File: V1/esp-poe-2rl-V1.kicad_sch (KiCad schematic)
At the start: 68 parts, among them J1 USB_C_Receptacle_USB2.0, J2 1x2P 5,08mm, J3 1x2P 5,08mm, J4 RJ45 JACK, K1 G5NB-1A-E-DC5, K2 G5NB-1A-E-DC5, Q1 WPM2015-3/TR, Q2 LMUN2211LT1G, Q3 UMH3N, Q4 MMBT2222A, Q5 MMBT2222A, SW1 RESET, U1 CH340K, U2 ESP32-WROOM-32UE-N16, U3 LAN8710A

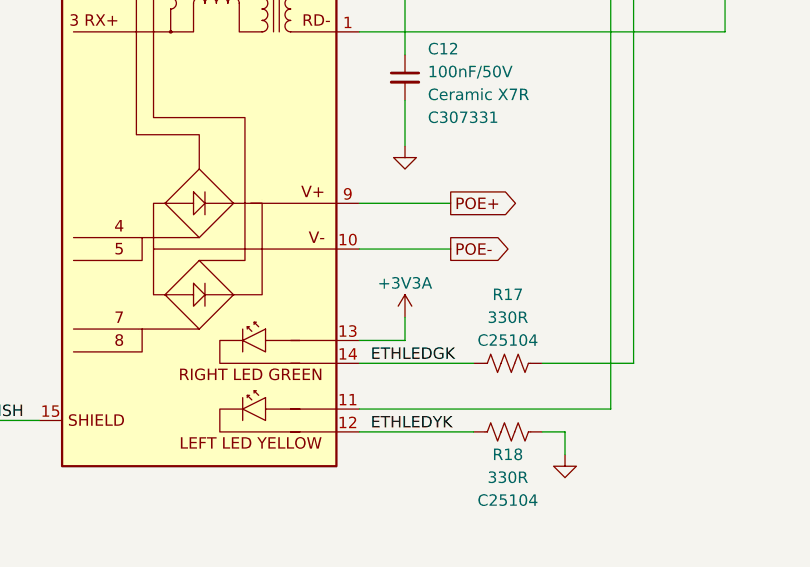
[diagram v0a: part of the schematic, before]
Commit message: Update power rail names
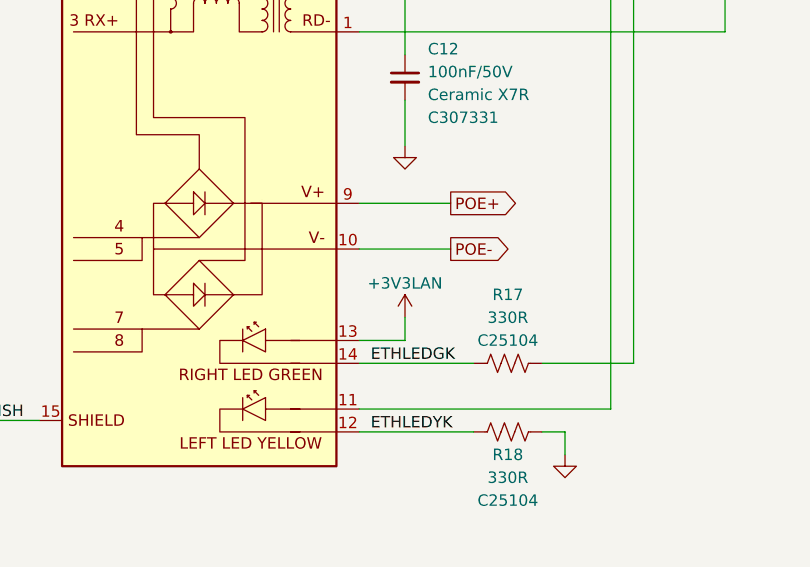
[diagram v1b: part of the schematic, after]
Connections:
- net +3V3A: no longer J4.13 (RLED+)
- net +3V3LAN: now also J4.13 (RLED+)
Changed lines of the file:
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@@
 	)
 	(symbol
+		(lib_id "Tales:+3V3LAN")
+		(at 336.55 219.71 0)
+		(unit 1)
+		(exclude_from_sim no)
+		(in_bom yes)
+		(on_board yes)
+		(dnp no)
+		(property "Reference" "#PWR042"
+			(at 336.55 223.52 0)
+			(effects
+				(font
+					(size 1.27 1.27)
+				)
+				(hide yes)
+			)
+		)
+		(property "Value" "+3V3LAN"
+			(at 336.55 215.9 0)
+			(effects
+				(font
+					(size 1.27 1.27)
+				)
+			)
+		)
+		(property "Footprint" ""
+			(at 336.55 219.71 0)
+			(effects
+				(font
+					(size 1.27 1.27)
+				)
+				(hide yes)
+			)
+		)
+		(property "Datasheet" ""
+			(at 336.55 219.71 0)
+			(effects
+				(font
+					(size 1.27 1.27)
+				)
+				(hide yes)
+			)
+		)
+		(property "Description" "Power symbol creates a global label with name \"+3V3LAN\""
+			(at 336.55 219.71 0)
+			(effects
+				(font
+					(size 1.27 1.27)
+				)
+				(hide yes)
+			)
+		)
+		(pin "1"
+		)
+		(instances
+			(project "esp-poe-2rl-V1"
+				(path "/2bc5a21a-1d79-419d-a592-6852cc07b00a"
+					(reference "#PWR042")
+					(unit 1)
+				)
+			)
+		)
+	)
+	(symbol
 		(lib_id "Device:R_US")
 		(at 242.57 38.1 0)
@@
 					(unit 1)
 				)
-			)
-		)
-	)
-	(symbol
-		(lib_id "Tales:+3V3A")
-		(at 336.55 219.71 0)
-		(unit 1)
-		(exclude_from_sim no)
-		(in_bom yes)
-		(on_board yes)
-		(dnp no)
-		(property "Reference" "#PWR042"
-			(at 336.55 223.52 0)
-			(effects
-				(font
-					(size 1.27 1.27)
-				)
-				(hide yes)
-			)
-		)
-		(property "Value" "+3V3A"
-			(at 336.55 215.9 0)
-			(effects
-				(font
-					(size 1.27 1.27)
-				)
-			)
-		)
-		(property "Footprint" ""
-			(at 336.55 219.71 0)
-			(effects
-				(font
-					(size 1.27 1.27)
-				)
-				(hide yes)
-			)
-		)
-		(property "Datasheet" ""
-			(at 336.55 219.71 0)
-			(effects
-				(font
-					(size 1.27 1.27)
-				)
-				(hide yes)
-			)
-		)
-		(property "Description" "Power symbol creates a global label with name \"+3V3A\""
-			(at 336.55 219.71 0)
-			(effects
-				(font
-					(size 1.27 1.27)
-				)
-				(hide yes)
-			)
-		)
-		(pin "1"
-		)
-		(instances
-			(project "esp-poe-2rl-V1"
-				(path "/2bc5a21a-1d79-419d-a592-6852cc07b00a"
-					(reference "#PWR042")
-					(unit 1)
-				)

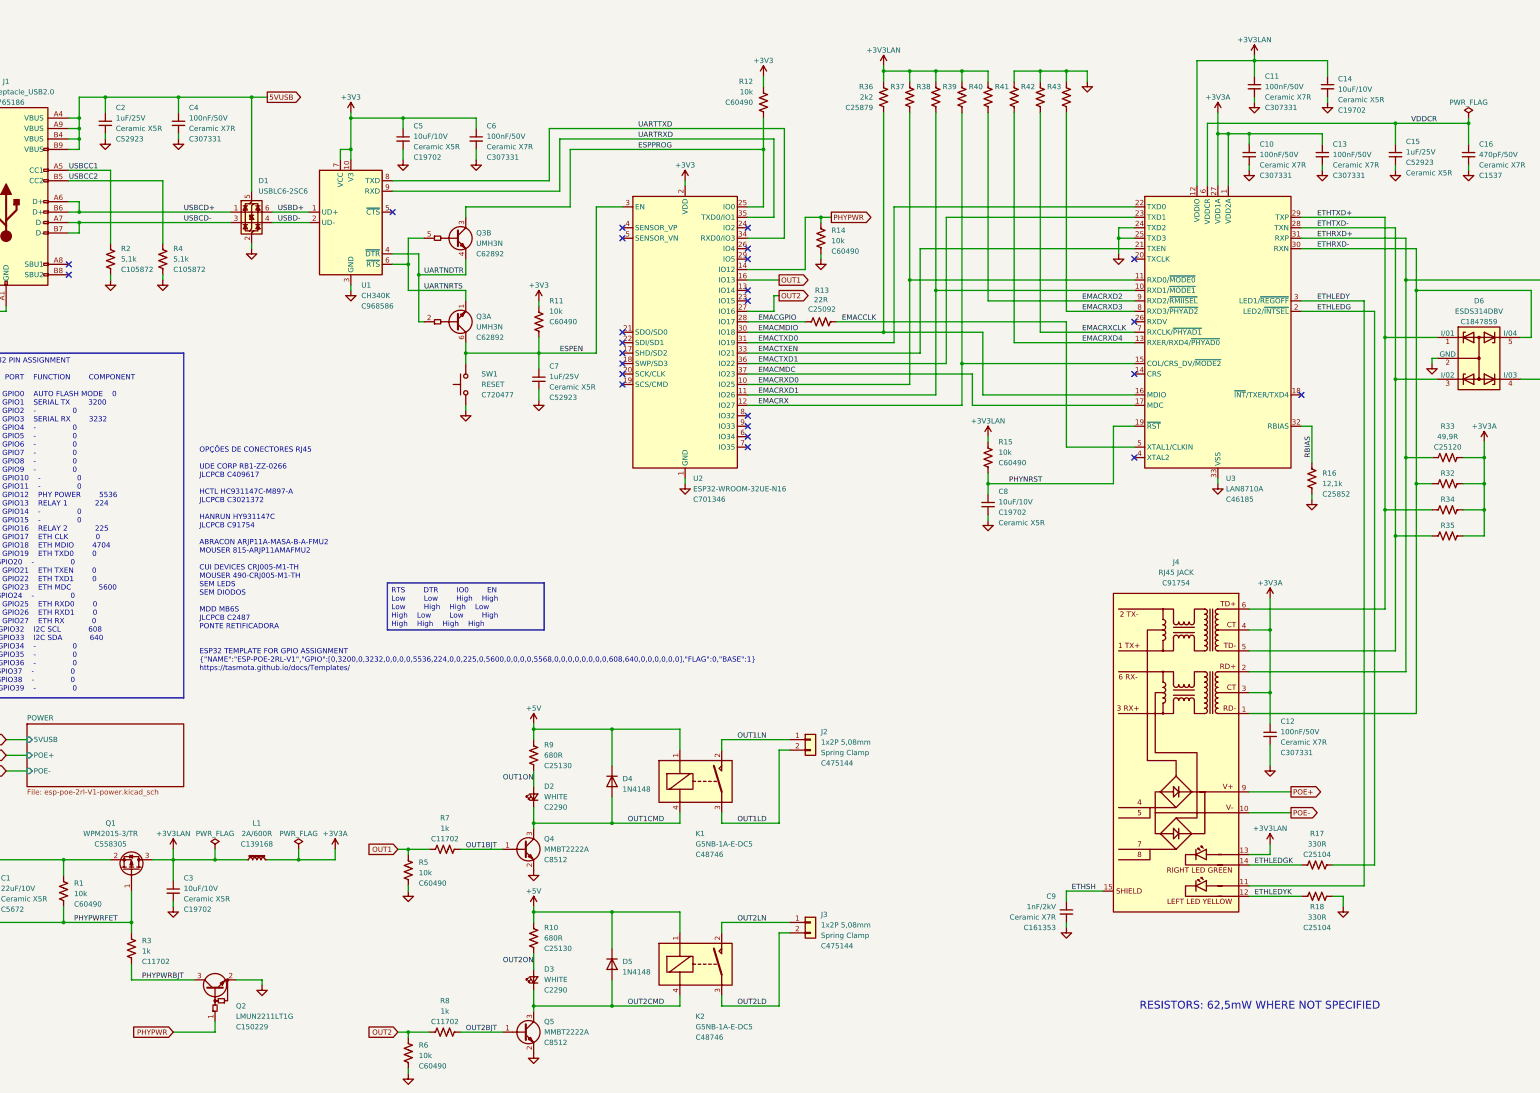
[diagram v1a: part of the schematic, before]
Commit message: addressing the PHY power rails
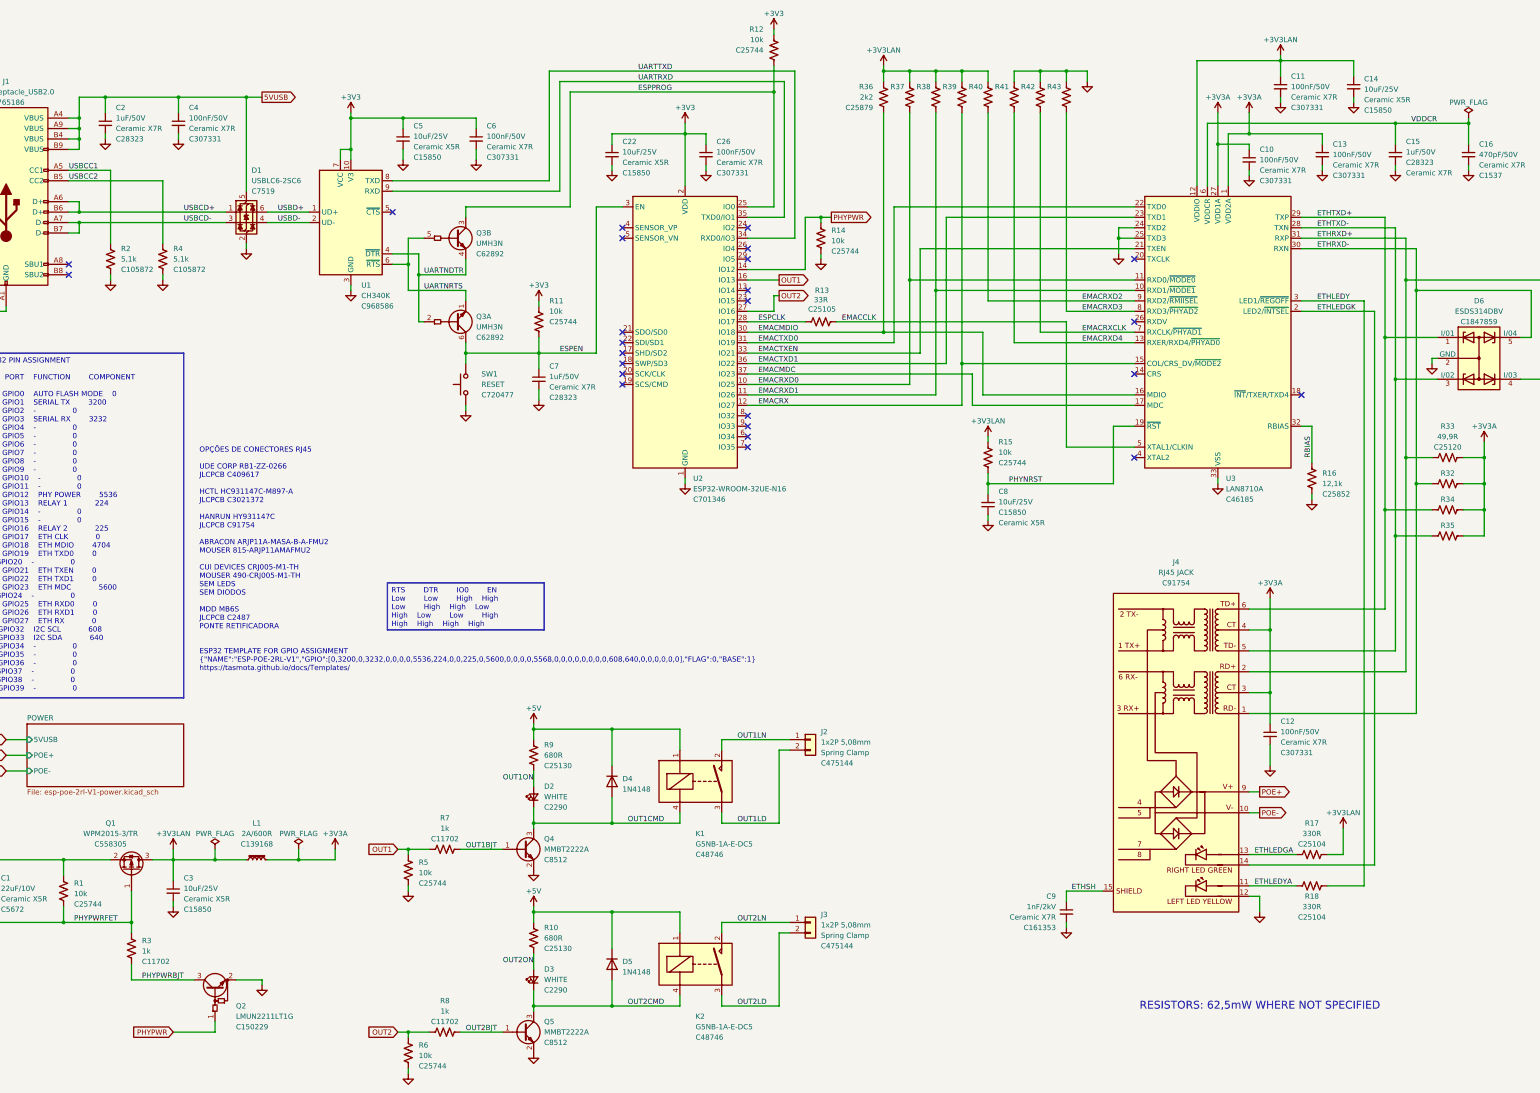
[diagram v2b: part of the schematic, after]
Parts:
- added C22: 10uF/25V, Tales:C_0805_2012Metric, symbol Device:C_Small
- added C26: 100nF/50V, Tales:C_0402_1005Metric, symbol Device:C_Small
- C14, C3, C5, C8: value 10uF/10V -> 10uF/25V; footprint Tales:C_0603_1608Metric -> Tales:C_0805_2012Metric; LCSC Part # C19702 -> C15850; Mfr PN CL10A106KP8NNNC -> CL21A106KAYNNNE; Package 0603/1608 -> 0805/2012; Vendor PN C19702 -> C15850
- C15, C2, C7: value 1uF/25V -> 1uF/50V; footprint Tales:C_0402_1005Metric -> Tales:C_0805_2012Metric; LCSC Part # C52923 -> C28323; Mfr PN CL05A105KA5NQNC -> CL21B105KBFNNNE; Package 0402/1005 -> 0805/2012; Technology Ceramic X5R -> Ceramic X7R; Vendor PN C52923 -> C28323
- R1: LCSC Part # C60490 -> C25744; Mfr Yageo -> Uniroyal; Mfr PN RC0402FR-0710KL -> 0402WGF1002TCE; Vendor PN C60490 -> C25744
- R11, R12, R14, R15, R5, R6: LCSC Part # C60490 -> C25744; Mfr Yageo -> Uniroyal
- R13: value 22R -> 33R; LCSC Part # C25092 -> C25105; Mfr PN 0402WGF220JTCE -> 0402WGF330JTCE; Vendor PN C25092 -> C25105
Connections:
- net +3V3: now also C22.1, C26.1
- net +3V3LAN: now also R17.2; no longer J4.13 (RLED+)
- net ETHLEDGK: now also U3.2 (LED2/~{INTSEL}); no longer R17.1
- net ETHLEDY: now also R18.2; no longer J4.11 (LLED+)
- net GND: now also J4.12 (LLED-), C22.2, C26.2; no longer R18.2
- net EMACGPIO renamed ESPCLK
- removed net ETHLEDG: R17.2, U3.2 (LED2/~{INTSEL})
- net ETHLEDYK renamed ETHLEDYA
- net ETHLEDYA: now also J4.11 (LLED+); no longer J4.12 (LLED-)
- new net ETHLEDGA: J4.13 (RLED+), R17.1
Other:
- moved on the sheet: C10, C11, C14, D1, R12, R17, R18

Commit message: Replaced terminal blocks
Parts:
- removed C22: 10uF/25V, Tales:C_0805_2012Metric, symbol Device:C_Small
- added C18: 100nF/50V, Tales:C_0402_1005Metric, symbol Device:C_Small
- added C19, C7: 10uF/25V, Tales:C_0805_2012Metric, symbol Device:C_Small
- J2: value 1x2P 5,08mm -> 250-202; footprint Tales:TerminalBlock_Dibo_DB142R-5.08-2P_1x02_P5.08mm_Horizontal -> Tales:TerminalBlock_Wago_250-202_1x02_P3.5mm_45Degree; LCSC Part # C475144 -> C2765061; Mfr Cixi Kefa Elec -> Wago; Mfr PN KF142R-5.08-2P -> 250-202; Vendor PN C475144 -> C2765061
- J4: renamed from J3; value 1x2P 5,08mm -> 250-202; footprint Tales:TerminalBlock_Dibo_DB142R-5.08-2P_1x02_P5.08mm_Horizontal -> Tales:TerminalBlock_Wago_250-202_1x02_P3.5mm_45Degree; LCSC Part # C475144 -> C2765061; Mfr Cixi Kefa Elec -> Wago; Mfr PN KF142R-5.08-2P -> 250-202; Vendor PN C475144 -> C2765061
- R1: renamed from R12; Mfr PN RC0402FR-0710KL -> 0402WGF1002TCE; Vendor PN C60490 -> C25744
- R10: renamed from R14; Mfr PN RC0402FR-0710KL -> 0402WGF1002TCE; Vendor PN C60490 -> C25744
- R13: renamed from R11; Mfr PN RC0402FR-0710KL -> 0402WGF1002TCE; Vendor PN C60490 -> C25744
- R14: renamed from R13; Package JLCPCB -> 0402/1005
- R15: Mfr PN RC0402FR-0710KL -> 0402WGF1002TCE; Vendor PN C60490 -> C25744
- R16: renamed from R33; Package (none) -> 0402/1005
- R18: renamed from R32; Package (none) -> 0402/1005
- R19: renamed from R34; Package (none) -> 0402/1005
- R2: renamed from R36; value 2k2 -> 10k; LCSC Part # C25879 -> C25744; Mfr PN 0402WGF2201TCE -> 0402WGF1002TCE; Package (none) -> 0402/1005; Vendor PN C25879 -> C25744
- R20: renamed from R35; Package (none) -> 0402/1005
- R23: renamed from R5; Mfr PN RC0402FR-0710KL -> 0402WGF1002TCE; Vendor PN C60490 -> C25744
- R3: renamed from R37; value 2k2 -> 10k; LCSC Part # C25879 -> C25744; Mfr PN 0402WGF2201TCE -> 0402WGF1002TCE; Package (none) -> 0402/1005; Vendor PN C25879 -> C25744
- R30: renamed from R6; Mfr PN RC0402FR-0710KL -> 0402WGF1002TCE; Vendor PN C60490 -> C25744
- R4: renamed from R38; value 2k2 -> 10k; LCSC Part # C25879 -> C25744; Mfr PN 0402WGF2201TCE -> 0402WGF1002TCE; Package (none) -> 0402/1005; Vendor PN C25879 -> C25744
- R5: renamed from R39; value 2k2 -> 10k; LCSC Part # C25879 -> C25744; Mfr PN 0402WGF2201TCE -> 0402WGF1002TCE; Package (none) -> 0402/1005; Vendor PN C25879 -> C25744
- R6: renamed from R40; value 2k2 -> 10k; LCSC Part # C25879 -> C25744; Mfr PN 0402WGF2201TCE -> 0402WGF1002TCE; Package (none) -> 0402/1005; Vendor PN C25879 -> C25744
- R7: renamed from R41; value 2k2 -> 10k; LCSC Part # C25879 -> C25744; Mfr PN 0402WGF2201TCE -> 0402WGF1002TCE; Package (none) -> 0402/1005; Vendor PN C25879 -> C25744
- R8: renamed from R42; value 2k2 -> 10k; LCSC Part # C25879 -> C25744; Mfr PN 0402WGF2201TCE -> 0402WGF1002TCE; Package (none) -> 0402/1005; Vendor PN C25879 -> C25744
- R9: renamed from R43; value 2k2 -> 10k; LCSC Part # C25879 -> C25744; Mfr PN 0402WGF2201TCE -> 0402WGF1002TCE; Package (none) -> 0402/1005; Vendor PN C25879 -> C25744
- renumbered C11 to C1, C15 to C10, C16 to C11, C10 to C12, C7 to C13, C8 to C14, C12 to C15, C1 to C16, C3 to C17, C14 to C2, C9 to C20, C2 to C3, C26 to C8, C13 to C9, D6 to D2, D4 to D3, D2 to D4, D3 to D6, J4 to J3, Q3 to Q1, Q4 to Q2, Q1 to Q3, Q2 to Q4, R2 to R11, R4 to R12, R16 to R17, R9 to R21, R7 to R22, R18 to R24, R1 to R25, R17 to R26, R10 to R27, R3 to R28, R8 to R29
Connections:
- net +3V3: now also C7.1
- net +3V3A: now also C19.1
- net +3V3LAN: now also J3.11 (LLED+), C18.1; no longer R26.2
- net ETHLEDGA: now also U3.3 (LED1/~{REGOFF}); no longer R26.1
- net ETHLEDGK: now also R26.2; no longer U3.2 (LED2/~{INTSEL})
- net ETHLEDY: now also U3.2 (LED2/~{INTSEL}); no longer U3.3 (LED1/~{REGOFF})
- net GND: now also R26.1, C18.2, C19.2, C7.2; no longer J3.12 (LLED-)
- net ETHLEDYA renamed ETHLEDYK
- net ETHLEDYK: now also J3.12 (LLED-); no longer J3.11 (LLED+)
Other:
- moved on the sheet: D3, D4, D5, D6, J2, J4, K1, K2, L1, Q2, Q5, R21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

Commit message: V1.5.0
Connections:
- net +3V3A: now also J3.11 (LLED+)
- net +3V3LAN: no longer J3.11 (LLED+)
- net ETHRXD-: now also D2.3 (I/02); no longer D2.5 (I/04)
- net ETHTXD-: now also D2.5 (I/04); no longer D2.3 (I/02)
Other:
- moved on the sheet: C14, R15
